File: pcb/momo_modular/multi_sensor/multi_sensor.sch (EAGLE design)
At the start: 38 parts, among them U1 MCP6001U, U10 SM5470-DIFF-PRESS-SENSOR, U2 16LF1847, U3 DUAL-BUFFER-OD-NC7WZ07, U4 LT1990, U5 2:1-MUX, U6 2:1-MUX, U7 AD8557-DIGITRIM-OPAMP, U8 2:1-MUX, U9 2:1-MUX

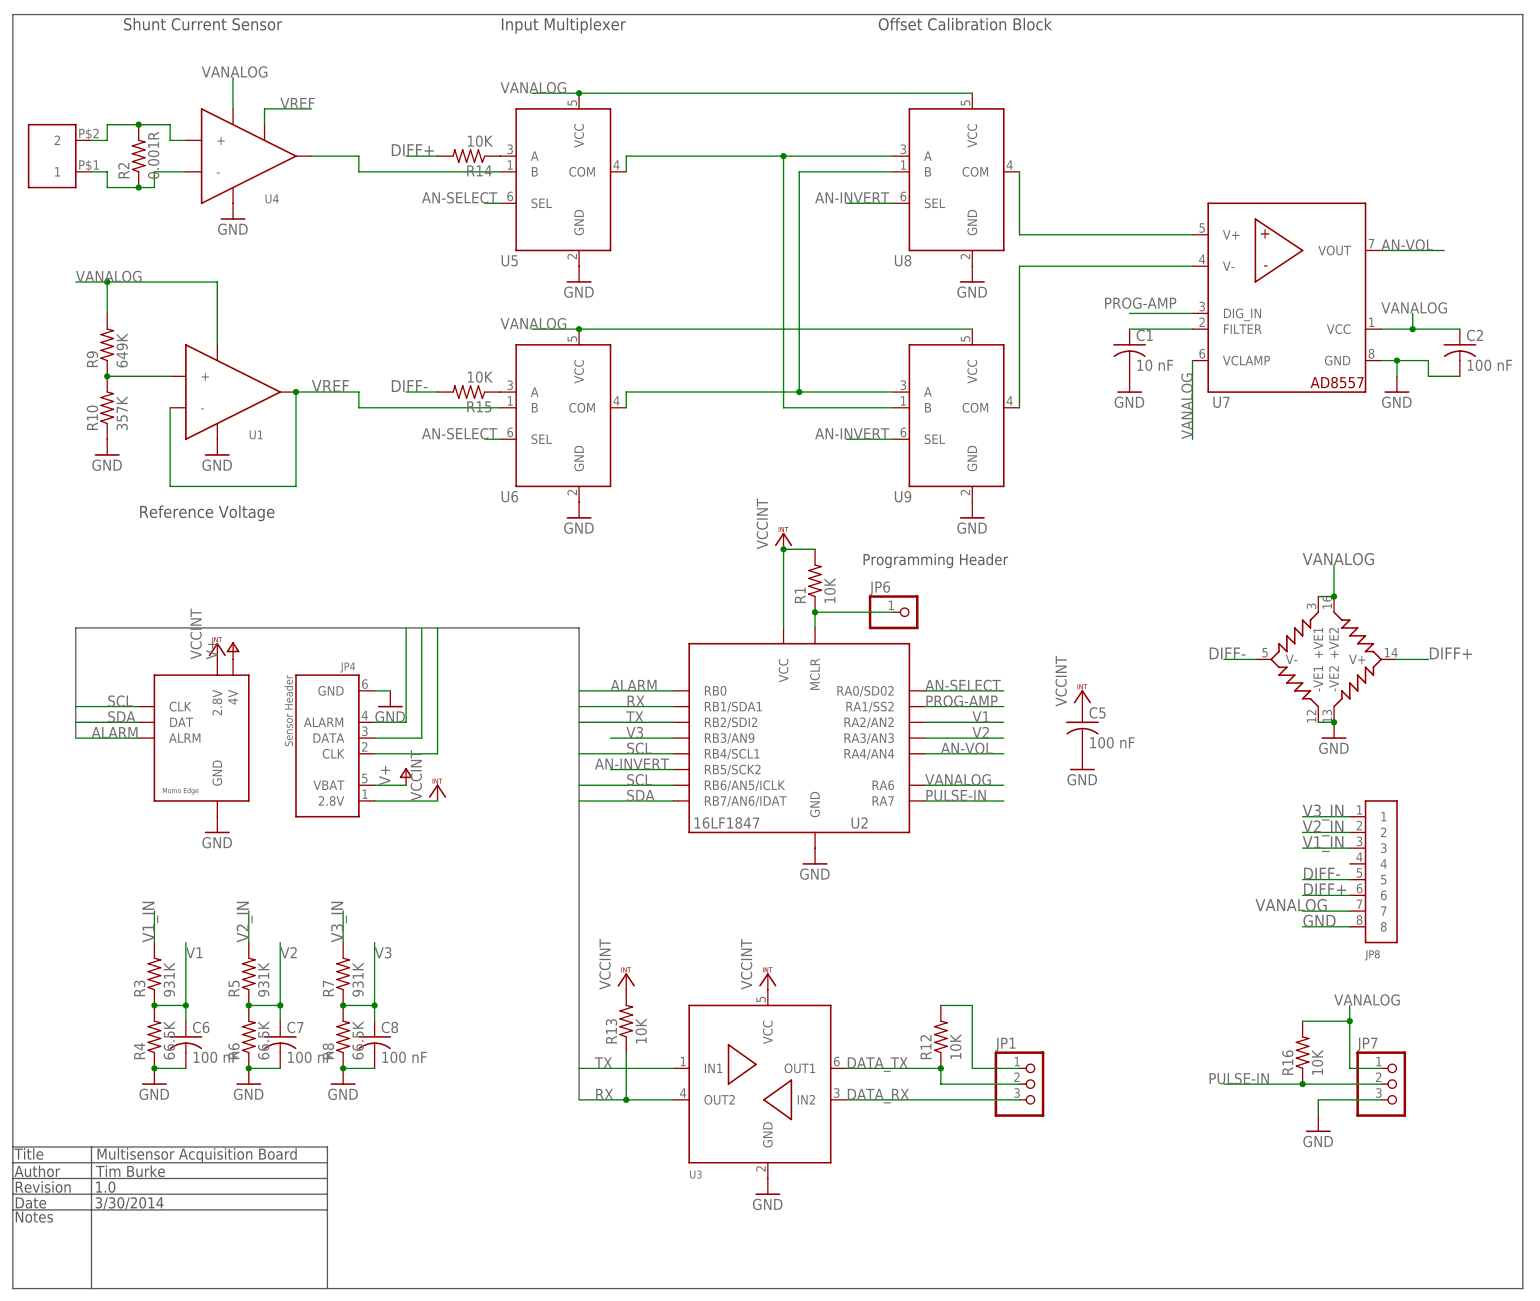
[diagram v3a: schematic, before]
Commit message: Fix multisensor board layout
- Add separate power supply for analog circuitry to
maintain voltage requirement.
- Fix data line connection on MIB bus
- Remove incorrect pin headers
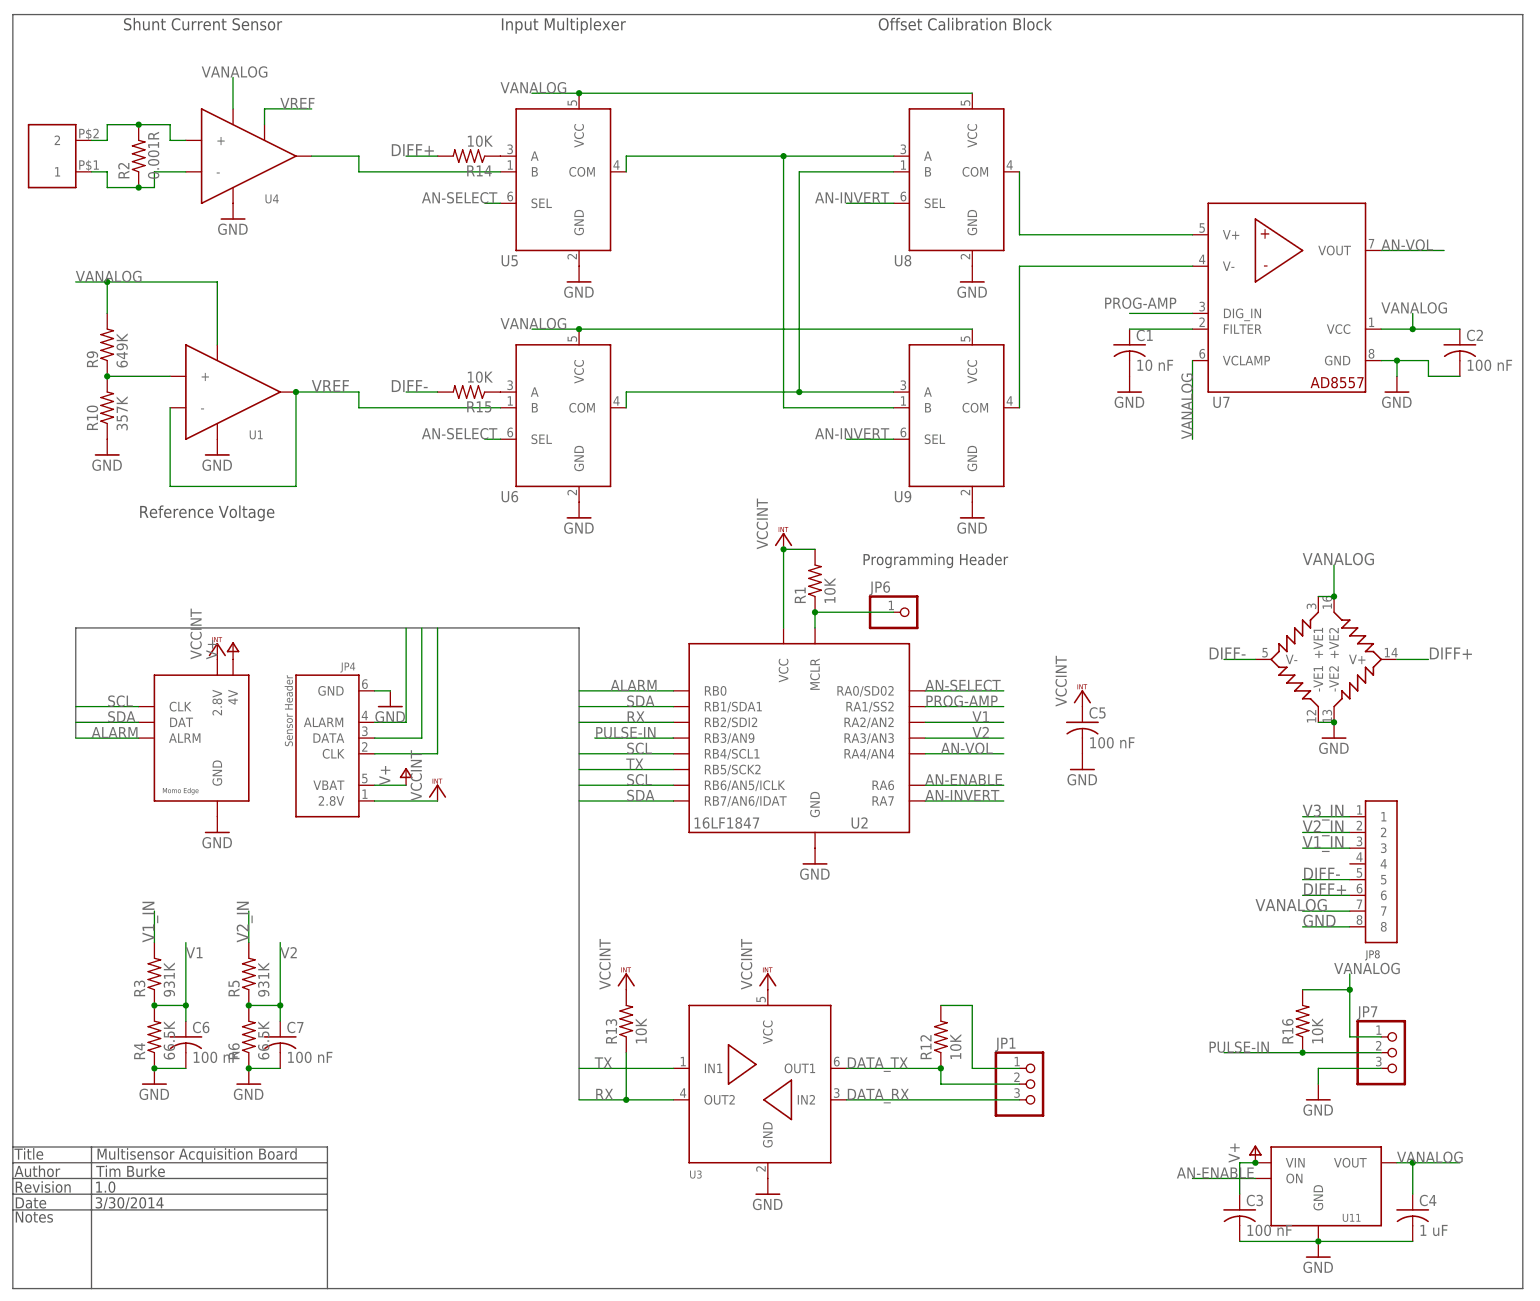
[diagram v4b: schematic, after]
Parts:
- removed C8: 100 nF, rcl:C-USC0402K
- removed R7: 931K, rcl:R-US_R0603
- removed R8: 66.5K, rcl:R-US_R0603
- added C3: 100 nF, rcl:C-USC0402K
- added C4: 1 uF, rcl:C-USC0402K
- added U11: TCR2EF28-LINREG, components:TCR2EF28-LINREG
- U10: POPULATE (none) -> no
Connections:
- removed net V3: C8.1, R7.1, R8.2, U2.RB3/AN9
- new net AN-ENABLE: U11.ON, U2.RA6
- net AN-INVERT: now also U2.RA7; no longer U2.RB5/SCK2
- net GND: now also C3.2, C4.2, U11.GND; no longer C8.2, R8.1
- net PULSE-IN: now also U2.RB3/AN9; no longer U2.RA7
- net RX: now also U2.RB2/SDI2; no longer U2.RB1/SDA1
- net SDA: now also U2.RB1/SDA1
- net TX: now also U2.RB5/SCK2; no longer U2.RB2/SDI2
- net V+: now also C3.1, U11.VIN
- net V3_IN: no longer R7.2
- net VANALOG: now also C4.1, U11.VOUT; no longer U2.RA6
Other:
- moved on the sheet: JP7, R16

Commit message: Update version numbers
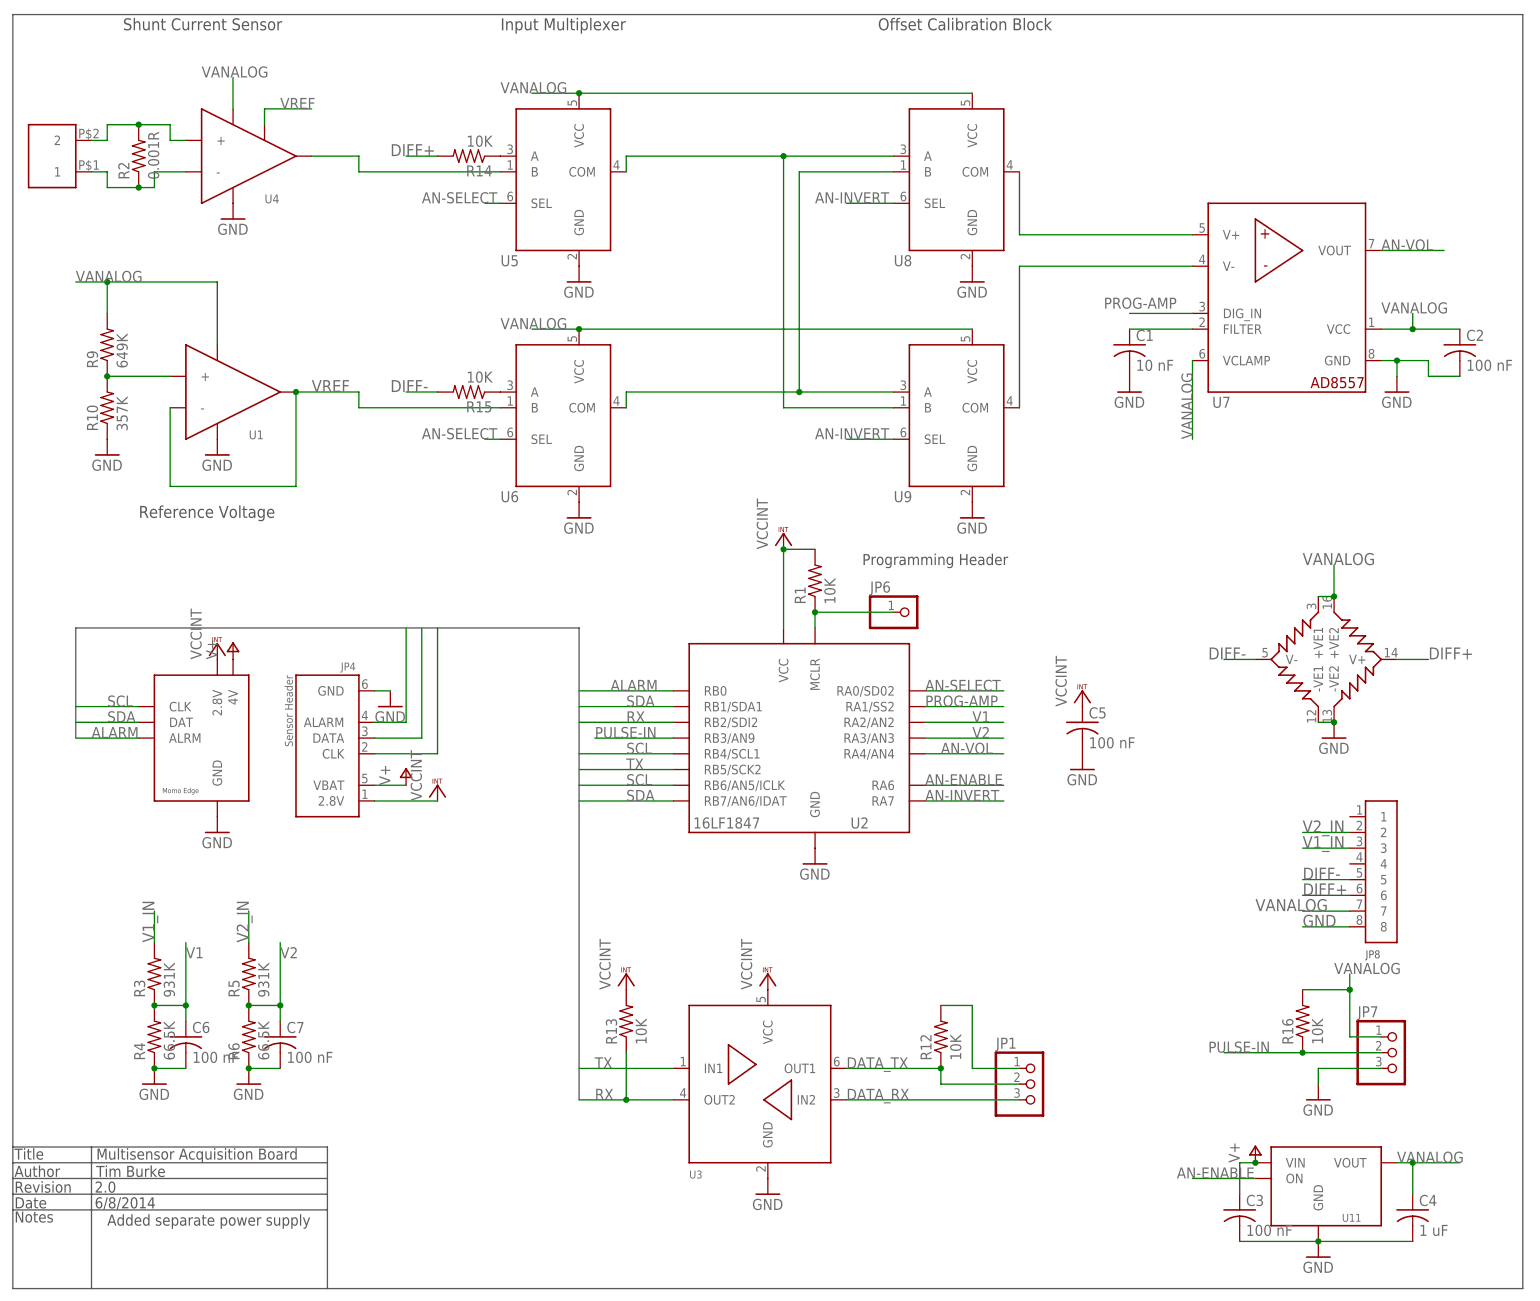
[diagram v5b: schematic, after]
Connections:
- removed net V3_IN: JP8.1
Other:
- note added: "2.0"
- note added: "6/8/2014"
- note added: "Added separate power supply"
- note removed: "1.0"
- note removed: "3/30/2014"
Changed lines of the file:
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@@
 <text x="-103.378" y="-88.392" size="1.778" layer="97">Multisensor Acquisition Board</text>
 <text x="-103.378" y="-91.186" size="1.778" layer="97">Tim Burke</text>
-<text x="-103.632" y="-93.726" size="1.778" layer="97">1.0</text>
-<text x="-103.632" y="-96.266" size="1.778" layer="97">3/30/2014</text>
+<text x="-103.632" y="-93.726" size="1.778" layer="97">2.0</text>
+<text x="-103.632" y="-96.266" size="1.778" layer="97">6/8/2014</text>
 <text x="20.32" y="7.62" size="1.778" layer="97">Programming Header</text>
 <text x="22.86" y="93.98" size="1.9304" layer="97">Offset Calibration Block</text>
@@
 <text x="-96.52" y="15.24" size="1.9304" layer="97">Reference Voltage</text>
 <wire x1="127" y1="96.52" x2="127" y2="-109.22" width="0.1524" layer="97"/>
+<text x="-101.6" y="-99.06" size="1.778" layer="97">Added separate power supply</text>
 </plain>
 <instances>
@@
 </segment>
 </net>
-<net name="V3_IN" class="0">
-<segment>
-<pinref part="JP8" gate="G$1" pin="1"/>
-<wire x1="99.06" y1="-33.02" x2="91.44" y2="-33.02" width="0.1524" layer="91"/>
-<label x="91.44" y="-33.02" size="1.9304" layer="95"/>
-</segment>
-</net>

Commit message: Add 3 pin headers for serial and turbine connector
Update RJ11 to different compatible model since the other was
backordered.
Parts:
- JP4: DIGIKEY-PN (none) -> AE10371-ND
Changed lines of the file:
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@@
 <part name="VCC6" library="supply1" deviceset="VCCINT" device=""/>
 <part name="GND11" library="supply1" deviceset="GND" device=""/>
-<part name="JP4" library="components" deviceset="MOMO-SENSOR-RJ11" device=""/>
+<part name="JP4" library="components" deviceset="MOMO-SENSOR-RJ11" device="">
+<attribute name="DIGIKEY-PN" value="AE10371-ND"/>
+</part>
 <part name="JP6" library="pinhead" deviceset="PINHD-1X1" device=""/>
 <part name="U1" library="components" deviceset="MCP6001U" device=""/>
